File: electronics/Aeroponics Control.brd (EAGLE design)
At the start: 87.3 x 71.1 mm, 37 parts, among them IC1 7407N, K1 SRM-1C-SL-5VDC, K2 SRM-1C-SL-5VDC, Q1 FDU3N40TU, Q2 FDU3N40TU, Q3 FDU3N40TU, Q4 FDU3N40TU, Q6 FDU3N40TU, Q7 FDU3N40TU

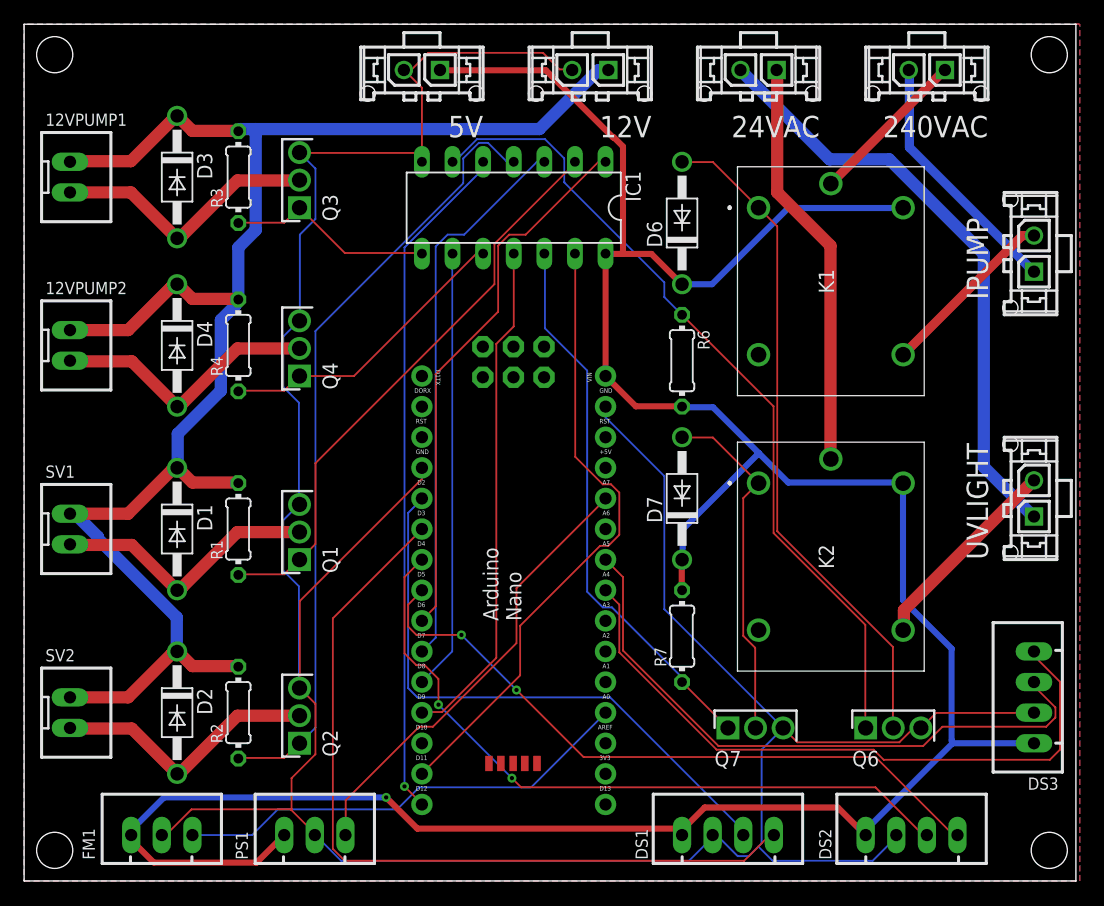
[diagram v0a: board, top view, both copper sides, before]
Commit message: Electronics tested. Added calibration and debug.
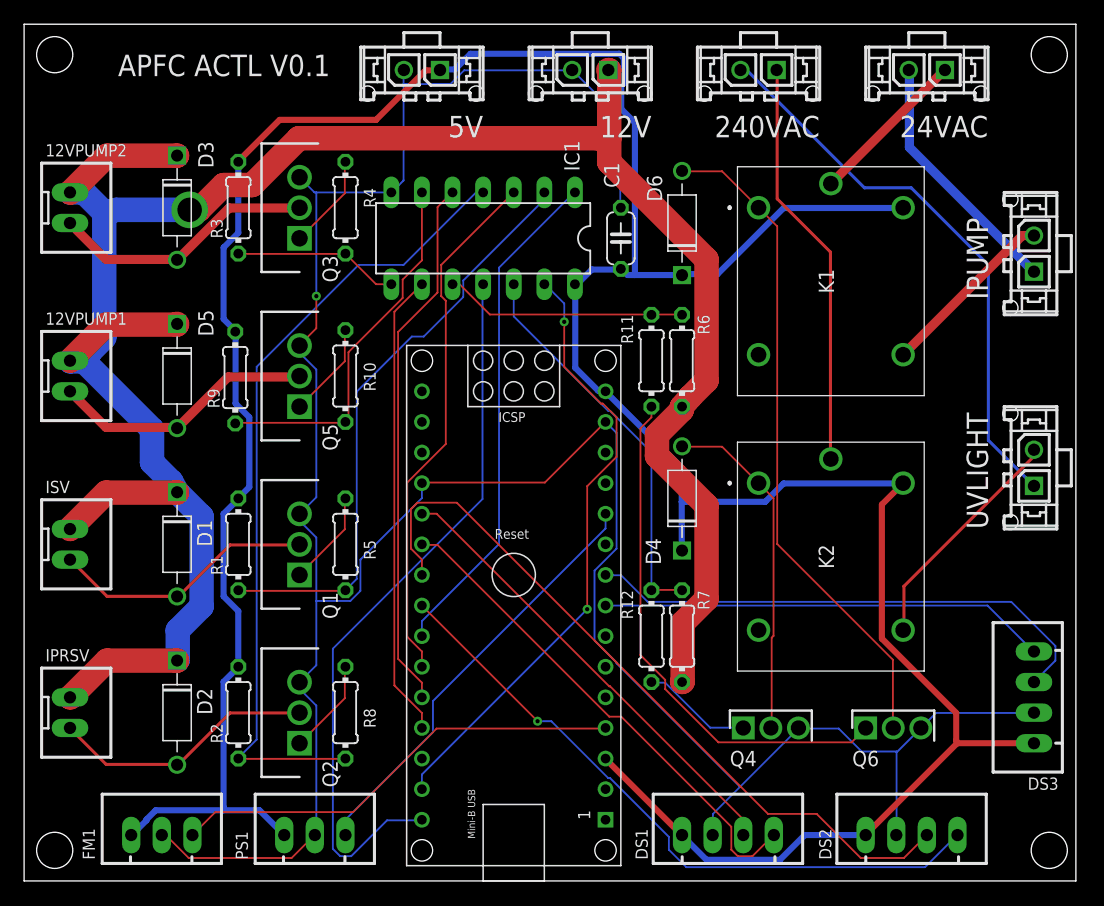
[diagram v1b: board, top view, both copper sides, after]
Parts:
- removed D7: 1N4004, diode:DO41-10
- removed Q7: FDU3N40TU, SamacSys_Parts:TO229P250X658X985-3P
- removed SV1, SV2: JST-XH-02-PIN-LONG-PAD, Rembrandt Electronics - JST XH Connectors v1-0:JST-XH-02-PACKAGE-LONG-PAD
- added C1: 100n, Aeroponics Control:C050-024X044
- added D5: 1N4004, Aeroponics Control:DO-41
- added IPRSV, ISV: JST-XH-02-PIN-LONG-PAD, Aeroponics Control:JST-XH-02-PACKAGE-LONG-PAD
- added Q5: FQP30N06L, Aeroponics Control:TO254P470X1016X2019-3P
- added R10, R11, R12, R5, R8: 1K, Aeroponics Control:0204/7
- added R9: 10k, Aeroponics Control:0204/7
- 12VPUMP1, 12VPUMP2: device Rembrandt Electronics - JST XH Connectors v1-0:JST-XH-02-PACKAGE-LONG-PAD -> Aeroponics Control:JST-XH-02-PACKAGE-LONG-PAD
- 12VS, 240ACVS, 24ACVS, 5VS, IPUMP, UVLIGHT: device con-molex-micro-fit-3_0:43650-0215 -> Aeroponics Control:43650-0215
- D1, D2, D3, D4, D6: device diode:DO41-10 -> Aeroponics Control:DO-41
- DS1, DS2, DS3: device Rembrandt Electronics - JST XH Connectors v1-0:JST-XH-04-PACKAGE-LONG-PAD -> Aeroponics Control:JST-XH-04-PACKAGE-LONG-PAD
- FM1, PS1: device Rembrandt Electronics - JST XH Connectors v1-0:JST-XH-03-PACKAGE-LONG-PAD -> Aeroponics Control:JST-XH-03-PACKAGE-LONG-PAD
- IC1: device 74xx-eu:DIL14 -> Aeroponics Control:DIL14
- K1, K2: device SamacSys_Parts:SRM1CSL5VDC -> Aeroponics Control:SRM1CSL5VDC
- PCB1: device E14_Arduino_revC:ARDUINO_NANO_HEADERS -> Aeroponics Control:ARDUINO_NANO
- Q1, Q2, Q3: value FDU3N40TU -> FQP30N06L; device SamacSys_Parts:TO229P250X658X985-3P -> Aeroponics Control:TO254P470X1016X2019-3P
- Q4, Q6: device SamacSys_Parts:TO229P250X658X985-3P -> Aeroponics Control:TO229P250X658X985-3P
- R1, R2, R3, R6, R7: device resistor:0204/7 -> Aeroponics Control:0204/7
- R4: value 10k -> 1K; device resistor:0204/7 -> Aeroponics Control:0204/7
- moved Q4 47.0 mm to (72.4, 12.7), turned to 0 degrees
- moved D4 43.8 mm to (67.3, 31.8), turned to 90 degrees
- moved PCB1 24.5 mm to (53.3, 25.4)
- moved 12VPUMP1 16.5 mm to (16.5, 41.9)
- moved R4 14.5 mm to (39.4, 55.9)
- moved 12VPUMP2 11.4 mm to (16.5, 55.9)
- moved IC1 3.59 mm to (50.8, 53.3)
- moved D3 2.54 mm to (25.4, 55.9)
- moved Q3 2.54 mm to (35.6, 53.3)
- moved R3 2.54 mm to (30.5, 55.9)
- moved UVLIGHT 2.54 mm to (96.5, 34.3)
- moved Q1 1.27 mm to (35.6, 25.4)
- moved D1 1.27 mm to (25.4, 27.9)
- moved R1 1.27 mm to (30.5, 27.9)
- turned R7 to 270 degrees
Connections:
- removed net N$23: IC1.6, Q6.1, R6.1
- removed net N$8 (its old number): IC1.12, Q7.1, R7.1
- removed net SV1CTL: IC1.1, PCB1.D6
- removed net SV2CTL: IC1.3, PCB1.D7
- new net 5V: PCB1.12
- new net IPRSVCTL: IC1.3, PCB1.25
- new net ISVCTL: IC1.1, PCB1.24
- new net N$14: 12VPUMP1.2, D5.A, Q5.2
- new net N$15: IC1.6, R10.1, R9.1
- new net N$16: Q5.1, R10.2
- new net N$17: IC1.10, R11.1, R6.1
- new net N$18: Q4.1, R12.2
- new net N$19: IC1.12, R12.1, R7.1
- new net N$5: Q1.1, R5.2
- new net N$9: IC1.4, R2.1, R8.1
- net +12V: now also D5.C, IPRSV.1, ISV.1, R6.2, R7.2; no longer D4.C, R1.2, R2.2, R3.2, R4.2, SV1.1, SV2.1
- net +5V: now also C1.1, D4.C, PCB1.15, PCB1.3, R1.2, R2.2, R3.2, R9.2; no longer D7.C, PCB1.VIN, R6.2, R7.2
- net DS1RX: now also PCB1.20; no longer PCB1.D2
- net DS1TX: now also PCB1.21; no longer PCB1.D3
- net DS2RX: now also PCB1.22; no longer PCB1.D4
- net DS2TX: now also PCB1.23; no longer PCB1.D5
- net DS3RX: now also PCB1.9; no longer PCB1.A5
- net DS3TX: now also PCB1.8; no longer PCB1.A4
- net FM1S: now also PCB1.4; no longer PCB1.A0
- net GND: now also C1.2, PCB1.14, PCB1.19, Q5.3; no longer PCB1.GND, PCB1.GND., Q7.3
- net IPCTL: now also IC1.11, PCB1.30; no longer IC1.5, PCB1.D12
- net N$1: now also IPRSV.2; no longer SV2.2
- net N$10: now also ISV.2; no longer SV1.2
- net N$11: now also IC1.8, R3.1, R4.1; no longer 12VPUMP1.2, D3.A, Q3.2
- net N$12: now also R4.2; no longer IC1.8, R3.1
- net N$13: now also Q6.1, R11.2; no longer 12VPUMP2.2, D4.A, Q4.2
- net N$2: now also 12VPUMP2.2, D3.A, Q3.2; no longer IC1.10, Q4.1, R4.1
- net N$3: now also R5.1; no longer Q1.1
- net N$4: now also R8.2; no longer IC1.4, R2.1
- net N$6: now also D4.A, Q4.2; no longer D7.A, Q7.2
- net PS1S: now also PCB1.11; no longer PCB1.A7
- net TP1CTL: now also IC1.5, PCB1.26; no longer IC1.9, PCB1.D8
- net TP2CTL: now also IC1.9, PCB1.27; no longer IC1.11, PCB1.D9
- net UVLCTL: now also PCB1.29; no longer PCB1.D11
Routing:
- net N$23: track 68.3 -> 0.00 mm
- net N$9: track 0.00 -> 66.9 mm
- net N$4: track 65.2 -> 7.95 mm
- net +12V: track 143.3 -> 190.8 mm, vias 0 -> 1
- net N$8 (its old number): track 46.1 -> 0.00 mm
- net SV2CTL: track 46.0 -> 0.00 mm
- net SV1CTL: track 45.6 -> 0.00 mm
- net IPRSVCTL: track 0.00 -> 43.9 mm
- net ISVCTL: track 0.00 -> 42.1 mm
- net +5V: track 229.5 -> 269.5 mm, vias 1 -> 0
- net N$19: track 0.00 -> 32.8 mm
- net N$15: track 0.00 -> 30.9 mm
- net DS1TX: track 67.5 -> 41.8 mm
- net GND: track 249.4 -> 226.9 mm, vias 0 -> 1
- net N$14: track 0.00 -> 22.1 mm
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- removed copper zone on layer 1, net GND
- removed copper zone on layer 16, net GND

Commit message: Updated aeroponics control electronics.
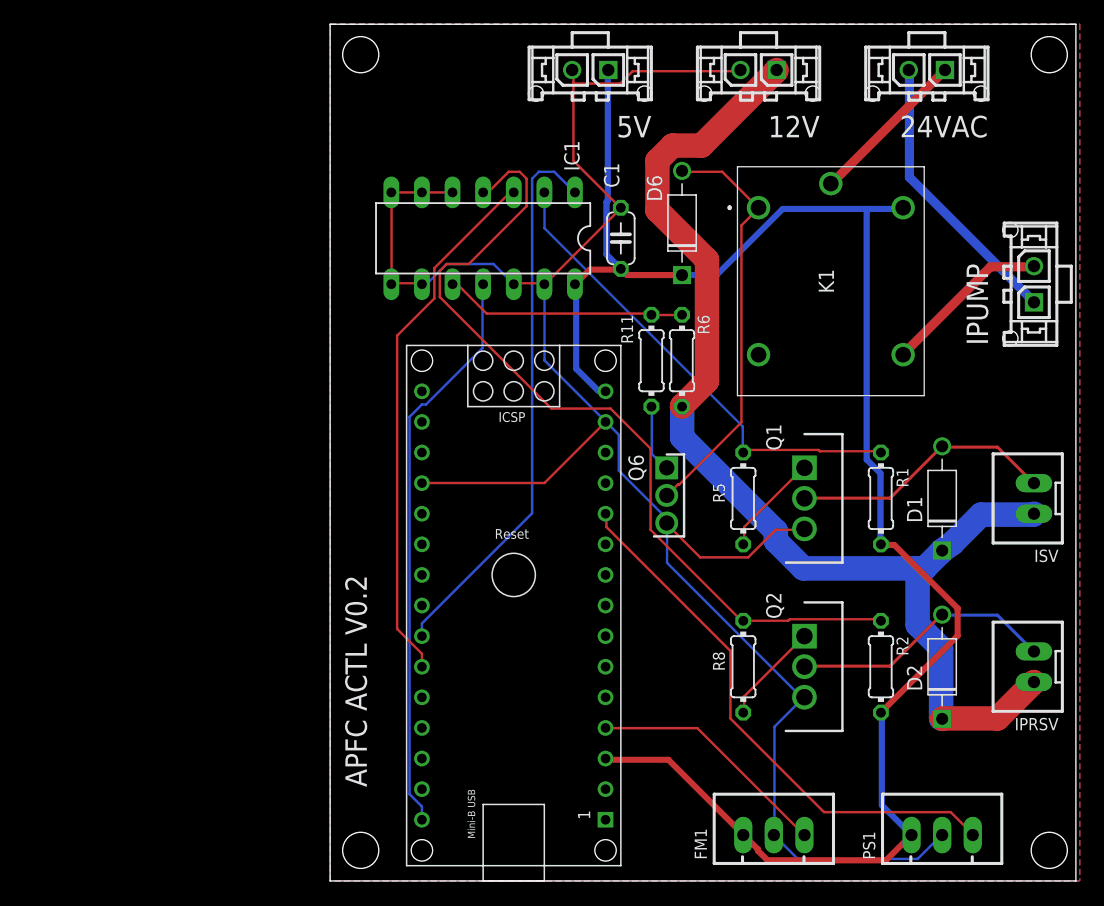
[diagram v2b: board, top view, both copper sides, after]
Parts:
- removed 12VPUMP1, 12VPUMP2: JST-XH-02-PIN-LONG-PAD, Aeroponics Control:JST-XH-02-PACKAGE-LONG-PAD
- removed 240ACVS, UVLIGHT: (no value), Aeroponics Control:43650-0215
- removed D3, D4, D5: 1N4004, Aeroponics Control:DO-41
- removed DS1, DS2, DS3: JST-XH-04-PIN-LONG-PAD, Aeroponics Control:JST-XH-04-PACKAGE-LONG-PAD
- removed K2: SRM-1C-SL-5VDC, Aeroponics Control:SRM1CSL5VDC
- removed Q3, Q5: FQP30N06L, Aeroponics Control:TO254P470X1016X2019-3P
- removed Q4: FDU3N40TU, Aeroponics Control:TO229P250X658X985-3P
- removed R10, R12, R4: 1K, Aeroponics Control:0204/7
- removed R3, R7, R9: 10k, Aeroponics Control:0204/7
- 12VS: value (none) -> 12VS
- 24ACVS: value (none) -> 24VACS
- 5VS: value (none) -> 5VS
- IPUMP: value (none) -> IPUMP
- moved IPRSV 80.1 mm to (96.5, 17.8), turned to 90 degrees
- moved ISV 80.1 mm to (96.5, 31.8), turned to 90 degrees
- moved D1 63.6 mm to (88.9, 31.8), turned to 90 degrees
- moved D2 63.6 mm to (88.9, 17.8), turned to 90 degrees
- moved R1 53.5 mm to (83.8, 31.8), turned to 270 degrees
- moved R2 53.5 mm to (83.8, 17.8), turned to 270 degrees
- moved PS1 52.1 mm to (88.9, 3.81)
- moved FM1 50.8 mm to (74.9, 3.81)
- moved Q1 42.8 mm to (77.5, 34.3), turned to 270 degrees
- moved Q2 42.8 mm to (77.5, 20.3), turned to 270 degrees
- moved R5 33.2 mm to (72.4, 31.8), turned to 270 degrees
- moved R8 33.2 mm to (72.4, 17.8), turned to 270 degrees
- moved Q6 27.2 mm to (66.0, 34.3), turned to 270 degrees
- moved 12VS 14.0 mm to (73.7, 67.3)
- moved 5VS 14.0 mm to (59.7, 67.3)
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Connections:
- removed net +240VAC: 240ACVS.P$1, K2.5
- removed net -240VAC: 240ACVS.P$2, UVLIGHT.P$1
- removed net DS1RX: DS1.3, PCB1.20
- removed net DS1TX: DS1.4, PCB1.21
- removed net DS2RX: DS2.3, PCB1.22
- removed net DS2TX: DS2.4, PCB1.23
- removed net DS3RX: DS3.3, PCB1.9
- removed net DS3TX: DS3.4, PCB1.8
- removed net N$11: IC1.8, R3.1, R4.1
- removed net N$12: Q3.1, R4.2
- removed net N$14: 12VPUMP1.2, D5.A, Q5.2
- removed net N$15: IC1.6, R10.1, R9.1
- removed net N$16: Q5.1, R10.2
- removed net N$18: Q4.1, R12.2
- removed net N$19: IC1.12, R12.1, R7.1
- removed net N$2: 12VPUMP2.2, D3.A, Q3.2
- removed net N$6: D4.A, K2.1, Q4.2
- removed net N$8: K2.3, UVLIGHT.P$2
- removed net TP1CTL: IC1.5, PCB1.26
- removed net TP2CTL: IC1.9, PCB1.27
- removed net UVLCTL: IC1.13, PCB1.29
- net +12V: no longer 12VPUMP1.1, 12VPUMP2.1, D3.C, D5.C, R7.2
- net +5V: no longer D4.C, DS1.1, DS2.1, DS3.1, K2.4, R3.2, R9.2
- net GND: now also IC1.12, IC1.13, IC1.5, IC1.6, IC1.8, IC1.9; no longer DS1.2, DS2.2, DS3.2, Q3.3, Q4.3, Q5.3
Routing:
- net +5V: track 269.5 -> 146.9 mm
- net +12V: track 190.8 -> 96.8 mm, vias 1 -> 0
- net DS2RX: track 61.9 -> 0.00 mm
- net GND: track 226.9 -> 166.1 mm, vias 1 -> 0
- net DS2TX: track 55.2 -> 0.00 mm, vias 1 -> 0
- net UVLCTL: track 51.2 -> 0.00 mm, vias 2 -> 0
- net -240VAC: track 47.2 -> 0.00 mm
- net TP1CTL: track 44.6 -> 0.00 mm
- net DS3RX: track 43.5 -> 0.00 mm
- net DS1TX: track 41.8 -> 0.00 mm
- net TP2CTL: track 38.7 -> 0.00 mm
- net DS1RX: track 38.5 -> 0.00 mm
- net N$13: track 43.6 -> 5.66 mm
- net DS3TX: track 37.1 -> 0.00 mm
- net +240VAC: track 34.2 -> 0.00 mm
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- added copper zone on layer 1, net GND
- added copper zone on layer 16, net GND
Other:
- board size 87.3 x 71.1 mm -> 61.9 x 71.1 mm
- board text added: "APFC ACTL V0.2"
- board text removed: "240VAC"
- board text removed: "APFC ACTL V0.1"
- board text removed: "UVLIGHT"

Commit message: Added pull down resistors to Arduino output pins
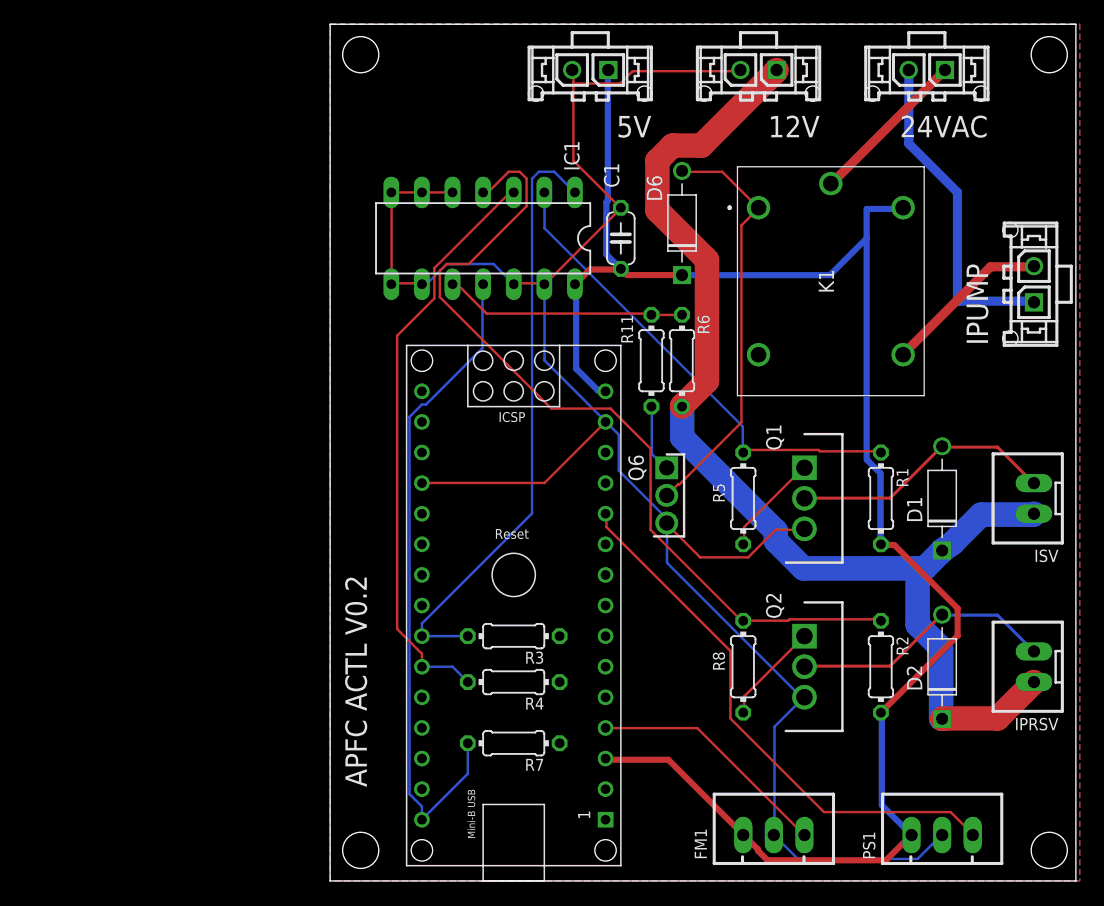
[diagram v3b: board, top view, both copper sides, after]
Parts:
- added R3, R4, R7: 10k, Aeroponics Control:0204/7
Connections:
- net GND: now also R3.1, R4.1, R7.1
- net IPCTL: now also R7.2
- net IPRSVCTL: now also R4.2
- net ISVCTL: now also R3.2
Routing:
- net IPCTL: track 47.6 -> 55.5 mm
- net IPRSVCTL: track 44.4 -> 48.7 mm
- net ISVCTL: track 46.3 -> 50.1 mm
- net -24VAC: track 23.6 -> 27.2 mm
- net +5V: track 146.9 -> 145.9 mm

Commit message: 8695xzbdw: Fix for flush valve opening on microcontroller reset
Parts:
- R3, R4, R7: value 10k -> 1k
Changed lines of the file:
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@@
 <grid distance="50" unitdist="mil" unit="mil" style="lines" multiple="1" display="no" altdistance="5" altunitdist="mil" altunit="mil"/>
 <layers>
-<layer number="1" name="Top" color="4" fill="1" visible="no" active="yes"/>
+<layer number="1" name="Top" color="4" fill="1" visible="yes" active="yes"/>
 <layer number="16" name="Bottom" color="1" fill="1" visible="yes" active="yes"/>
 <layer number="17" name="Pads" color="2" fill="1" visible="yes" active="yes"/>
@@
 <layer number="19" name="Unrouted" color="6" fill="1" visible="yes" active="yes"/>
 <layer number="20" name="Dimension" color="24" fill="1" visible="yes" active="yes"/>
-<layer number="21" name="tPlace" color="7" fill="1" visible="no" active="yes"/>
+<layer number="21" name="tPlace" color="7" fill="1" visible="yes" active="yes"/>
 <layer number="22" name="bPlace" color="7" fill="1" visible="yes" active="yes"/>
-<layer number="23" name="tOrigins" color="15" fill="1" visible="no" active="yes"/>
+<layer number="23" name="tOrigins" color="15" fill="1" visible="yes" active="yes"/>
 <layer number="24" name="bOrigins" color="15" fill="1" visible="yes" active="yes"/>
-<layer number="25" name="tNames" color="7" fill="1" visible="no" active="yes"/>
+<layer number="25" name="tNames" color="7" fill="1" visible="yes" active="yes"/>
 <layer number="26" name="bNames" color="7" fill="1" visible="yes" active="yes"/>
 <layer number="27" name="tValues" color="7" fill="1" visible="no" active="yes"/>
@@
 <layer number="37" name="tTest" color="7" fill="1" visible="no" active="yes"/>
 <layer number="38" name="bTest" color="7" fill="1" visible="no" active="yes"/>
-<layer number="39" name="tKeepout" color="4" fill="11" visible="no" active="yes"/>
+<layer number="39" name="tKeepout" color="4" fill="11" visible="yes" active="yes"/>
 <layer number="40" name="bKeepout" color="1" fill="11" visible="yes" active="yes"/>
-<layer number="41" name="tRestrict" color="4" fill="10" visible="no" active="yes"/>
+<layer number="41" name="tRestrict" color="4" fill="10" visible="yes" active="yes"/>
 <layer number="42" name="bRestrict" color="1" fill="10" visible="yes" active="yes"/>
 <layer number="43" name="vRestrict" color="2" fill="10" visible="no" active="yes"/>
@@
 <layer number="49" name="Reference" color="7" fill="1" visible="no" active="yes"/>
 <layer number="50" name="dxf" color="7" fill="1" visible="no" active="no"/>
-<layer number="51" name="tDocu" color="7" fill="1" visible="no" active="yes"/>
+<layer number="51" name="tDocu" color="7" fill="1" visible="yes" active="yes"/>
 <layer number="52" name="bDocu" color="7" fill="1" visible="yes" active="yes"/>
 <layer number="53" name="tGND_GNDA" color="7" fill="9" visible="no" active="no"/>
@@
 <attribute name="VALUE" x="57.531" y="53.975" size="1.27" layer="27" ratio="10" rot="R180"/>
 </element>
-<element name="R3" library="Aeroponics Control" package="0204/7" package3d_urn="urn:adsk.eagle:package:23498/2" value="10k" x="53.34" y="20.32" smashed="yes" rot="R180">
+<element name="R3" library="Aeroponics Control" package="0204/7" package3d_urn="urn:adsk.eagle:package:23498/2" value="1k" x="53.34" y="20.32" smashed="yes" rot="R180">
 <attribute name="NAME" x="55.88" y="19.0246" size="0.9906" layer="25" ratio="10" rot="R180"/>
 <attribute name="VALUE" x="54.9656" y="20.8026" size="0.9906" layer="27" ratio="10" rot="R180"/>
 </element>
-<element name="R4" library="Aeroponics Control" package="0204/7" package3d_urn="urn:adsk.eagle:package:23498/2" value="10k" x="53.34" y="16.51" smashed="yes" rot="R180">
+<element name="R4" library="Aeroponics Control" package="0204/7" package3d_urn="urn:adsk.eagle:package:23498/2" value="1k" x="53.34" y="16.51" smashed="yes" rot="R180">
 <attribute name="NAME" x="55.88" y="15.2146" size="0.9906" layer="25" ratio="10" rot="R180"/>
 <attribute name="VALUE" x="54.9656" y="16.9926" size="0.9906" layer="27" ratio="10" rot="R180"/>
 </element>
-<element name="R7" library="Aeroponics Control" package="0204/7" package3d_urn="urn:adsk.eagle:package:23498/2" value="10k" x="53.34" y="11.43" smashed="yes" rot="R180">
+<element name="R7" library="Aeroponics Control" package="0204/7" package3d_urn="urn:adsk.eagle:package:23498/2" value="1k" x="53.34" y="11.43" smashed="yes" rot="R180">
 <attribute name="NAME" x="55.88" y="10.1346" size="0.9906" layer="25" ratio="10" rot="R180"/>
 <attribute name="VALUE" x="54.9656" y="11.9126" size="0.9906" layer="27" ratio="10" rot="R180"/>
